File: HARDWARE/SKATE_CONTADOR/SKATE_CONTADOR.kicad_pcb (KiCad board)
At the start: 2 copper layers, 21 parts, among them J1 ENTRADA, J2 DISPLAY, SW1 INTERRUPTOR, SW2 VELOCIDAD, SW4 VELOCIDAD, U1 ESP32-DEVKIT-V1, U2 L7805

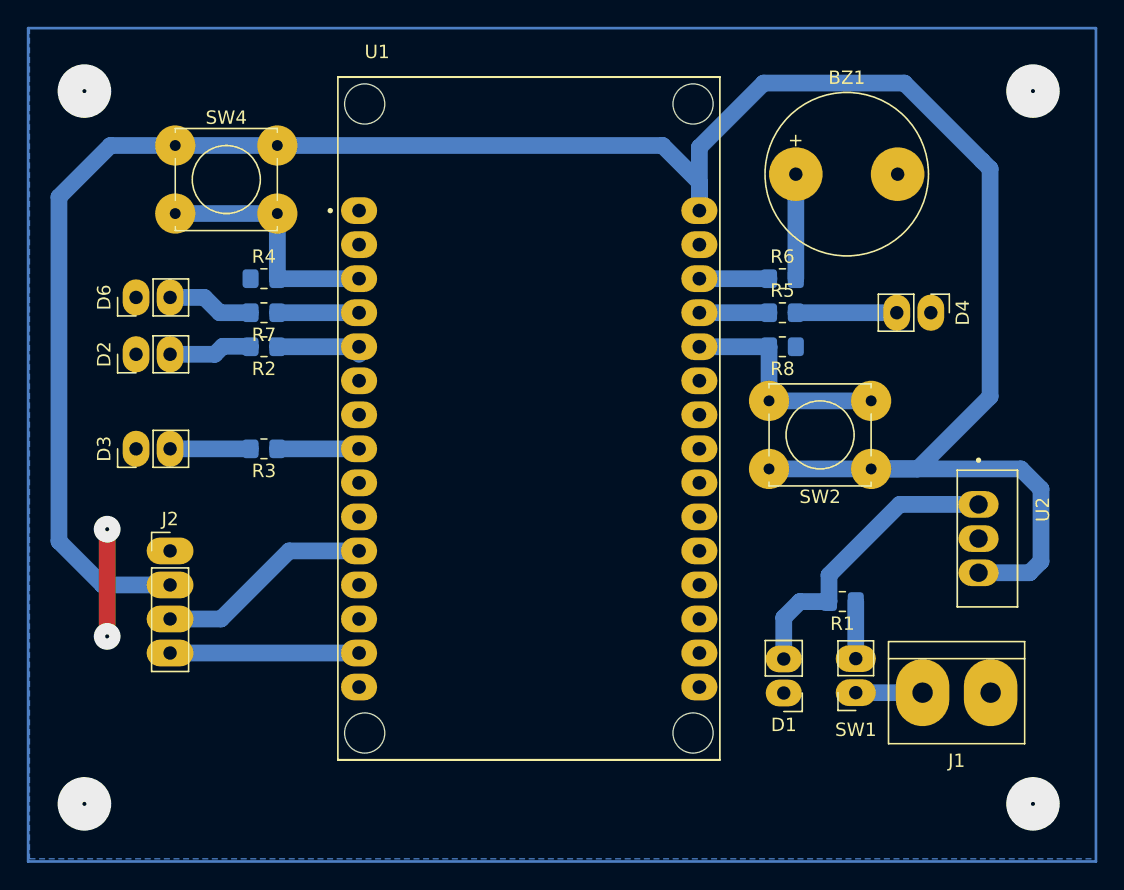
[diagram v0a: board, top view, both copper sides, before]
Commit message: capacitores de filtro
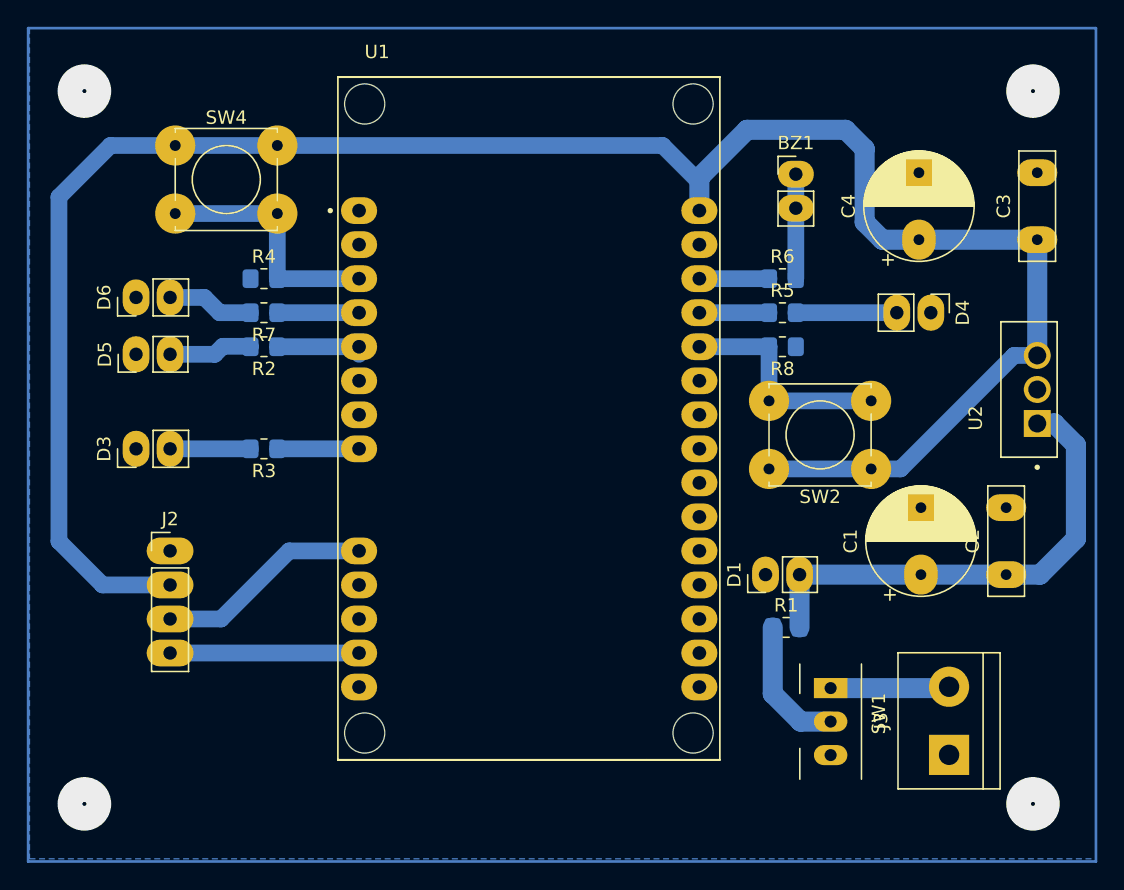
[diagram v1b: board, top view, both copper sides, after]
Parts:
- removed D2: LED, Connector_PinHeader_2.54mm:PinHeader_1x02_P2.54mm_Vertical
- removed J1: ENTRADA, TerminalBlock:TerminalBlock_bornier-2_P5.08mm
- added C1: C_Polarized_US, Capacitor_THT:CP_Radial_D8.0mm_P5.00mm, F.Cu at (89.6, 61.1)
- added C2: C, Capacitor_THT:C_Disc_D8.0mm_W2.5mm_P5.00mm, F.Cu at (95.9, 61.1)
- added C3: C, Capacitor_THT:C_Disc_D8.0mm_W2.5mm_P5.00mm, F.Cu at (98.2, 36.1)
- added C4: C_Polarized_US, Capacitor_THT:CP_Radial_D8.0mm_P5.00mm, F.Cu at (89.4, 36.1)
- added D5: LED, Connector_PinHeader_2.54mm:PinHeader_1x02_P2.54mm_Vertical, F.Cu at (31.0, 44.7)
- added J3: ENTRADA, TerminalBlock:TerminalBlock_bornier-2_P5.08mm, F.Cu at (91.7, 74.6)
- BZ1: footprint Buzzer_Beeper:Buzzer_12x9.5RM7.6 -> Connector_PinHeader_2.54mm:PinHeader_1x02_P2.54mm_Vertical
- SW1: footprint Connector_PinSocket_2.54mm:PinSocket_1x02_P2.54mm_Vertical -> Button_Switch_THT:SW_Slide_SPDT_Angled_CK_OS102011MA1Q
- U2: footprint L7805:TO255P1020X450X2000-3 -> LM7805C:TO254P1011X419X2286-3
- moved U2 11.6 mm to (97.6, 47.3), turned to 90 degrees
- moved D1 8.94 mm to (78.0, 61.1), turned to 90 degrees
- moved R1 4.62 mm to (79.5, 65.1), turned to 0 degrees
- moved SW1 1.88 mm to (82.8, 70.1), turned to -90 degrees
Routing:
- net +5V: track 178.5 -> 155.9 mm
- net Net-(D1-A): track 22.3 -> 36.2 mm
- net GND: track 8.00 -> 0.00 mm, vias 6 -> 4
- net Net-(SW1-B): track 4.26 -> 10.1 mm
- net Net-(J3-Pin_2): track 4.98 -> 8.88 mm
